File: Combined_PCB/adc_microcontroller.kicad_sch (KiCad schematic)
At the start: 26 parts, among them J3 Conn_01x18_Pin, J5 Conn_01x18_Pin, U1 ADS1299IPAG, U2 MCP1640BT-I/CHY

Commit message: Semi-finalized PCB Layout final
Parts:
- removed C15, C4: 1uF, Capacitor_SMD:C_0805_2012Metric, symbol Device:C
- removed C18, C8: .1uF, Capacitor_SMD:C_0805_2012Metric, symbol Device:C
- added R4: 1M, Resistor_SMD:R_0805_2012Metric, symbol Device:R
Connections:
- net AVDD is gone; now on net 5v: C14.1, C17.1, U1.19 (AVDD@1), U1.21 (AVDD@1), U1.22 (AVDD@1), U1.54 (AVDD1), U1.56 (AVDD@1), U1.59 (AVDD@2)
- net 3v3: now also C3.1, C7.1, U1.35 (~{PWDN}), U1.48 (DVDD), U1.50 (DVDD), R4.2
- net 5v: now also C20.1, R3.2; no longer C20.2, R3.1
- net AGND: now also C20.2, U1.17 (SRB1), U1.18 (SRB2), U1.25 (VREFN), U1.31 (RESV1); no longer C20.1
- net DRDY: now also J5.16 (Pin_16); no longer J5.15 (Pin_15)
- net START: now also J3.11 (Pin_11)
- net VREFP: now also U1.24 (VREFP)
- net at R2.1, U2.4 (VFB): now also R3.1; no longer R3.2
- net DAISY_IN: now reaches U1.41 (DAISY_IN)
- net GPIO1: now reaches U1.42 (GPIO1)
- net GPIO1: now also J3.16 (Pin_16)
- net GPIO2: now reaches U1.44 (GPIO2)
- net GPIO2: now also J3.15 (Pin_15)
- net GPIO3: now reaches U1.45 (GPIO3)
- net GPIO3: now also J3.14 (Pin_14)
- net GPIO4: now reaches U1.46 (GPIO4)
- net GPIO4: now also J3.13 (Pin_13)
- net CLK: no longer names the net of U1.37 (CLK)
- removed net DVDD: C3.1, C7.1, U1.35 (~{PWDN}), U1.48 (DVDD), U1.50 (DVDD), U1.52 (CLKSEL)
- new net CLK_SEL: R4.1, U1.52 (CLKSEL)
- no-connect marks 39 -> 25
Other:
- moved on the sheet: C1, C10, C12, C13, C14, C16, C17, C19, C2, C20, C3, C5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

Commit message: Schematic and footprints complete
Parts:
- removed U2: MCP1640BT-I/CHY, SOT-23-6_MC_MCH, symbol 2025-03-06_16-07-10:MCP1640BT-I_CHY
- added U7: MCP1640BT-I/CHY, MCP1640:SOT-23-6_MC_MCH, symbol MCP1640BT:MCP1640BT-I_CHY
- J6: renamed from J3; footprint (none) -> Connector_PinHeader_2.54mm:PinHeader_1x18_P2.54mm_Vertical
- J7: renamed from J5; footprint (none) -> Connector_PinHeader_2.54mm:PinHeader_1x18_P2.54mm_Vertical
- L1: footprint (none) -> Inductor_SMD:L_0805_2012Metric
- R3: renamed from R2; footprint (none) -> Resistor_SMD:R_0805_2012Metric
- R4: renamed from R3; footprint (none) -> Resistor_SMD:R_0805_2012Metric
- renumbered C1 to C11, C14 to C13, C13 to C14, C17 to C15, C2 to C17, C19 to C18, C20 to C19, C3 to C6, C5 to C8, C6 to C9, R4 to R2, U1 to U6
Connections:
- net 3v3: now also U7.3 (EN), U7.6 (VIN)
- net 5v: now also U7.5 (VOUT)
- net AGND: now also U7.2 (GND)
- net at L1.1: now also U7.1 (SW)
- net at R3.1, R4.1: now also U7.4 (VFB)
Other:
- moved on the sheet: U6

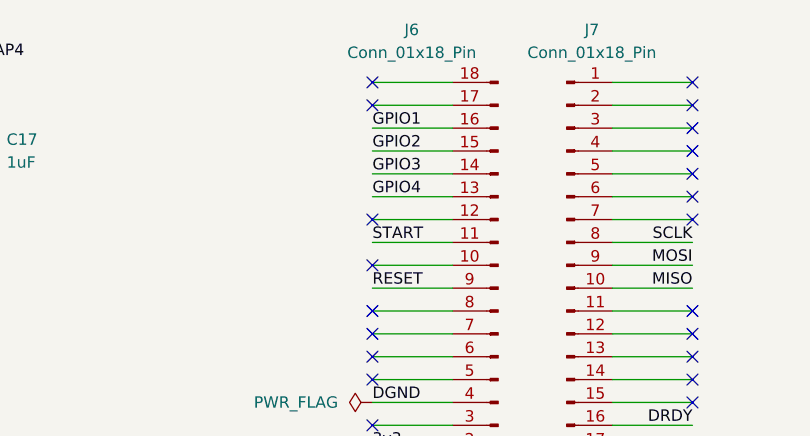
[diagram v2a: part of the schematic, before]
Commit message: ADS1299 final pcb layout done (hopefully)
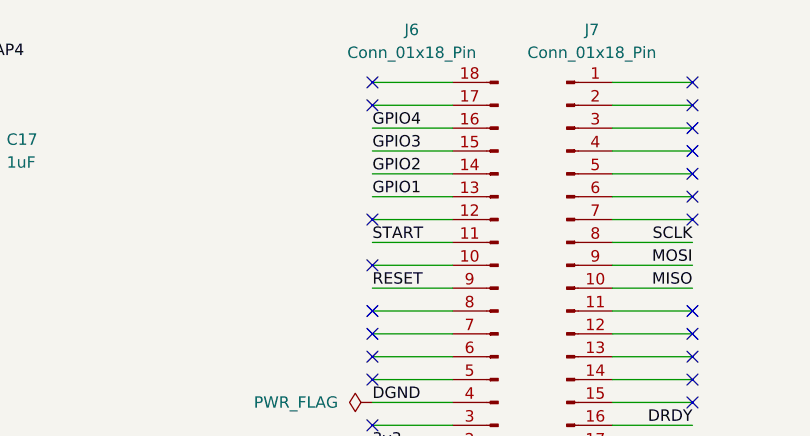
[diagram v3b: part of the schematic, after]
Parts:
- J6, J7: footprint Connector_PinHeader_2.54mm:PinHeader_1x18_P2.54mm_Vertical -> Connector_PinSocket_2.54mm:PinSocket_1x18_P2.54mm_Vertical
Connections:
- net GPIO1: now also J6.13 (Pin_13); no longer J6.16 (Pin_16)
- net GPIO2: now also J6.14 (Pin_14); no longer J6.15 (Pin_15)
- net GPIO3: now also J6.15 (Pin_15); no longer J6.14 (Pin_14)
- net GPIO4: now also J6.16 (Pin_16); no longer J6.13 (Pin_13)
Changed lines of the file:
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@@
 	)
 	(label "GPIO4"
-		(at 220.98 40.64 0)
+		(at 220.98 33.02 0)
 		(effects
 			(font
@@
 	)
 	(label "GPIO1"
-		(at 220.98 33.02 0)
+		(at 220.98 40.64 0)
 		(effects
 			(font
@@
 	)
 	(label "GPIO2"
-		(at 220.98 35.56 0)
+		(at 220.98 38.1 0)
 		(effects
 			(font
@@
 	)
 	(label "GPIO3"
-		(at 220.98 38.1 0)
+		(at 220.98 35.56 0)
 		(effects
 			(font
@@
 			)
 		)
-		(property "Footprint" "Connector_PinHeader_2.54mm:PinHeader_1x18_P2.54mm_Vertical"
+		(property "Footprint" "Connector_PinSocket_2.54mm:PinSocket_1x18_P2.54mm_Vertical"
 			(at 242.57 48.26 0)
 			(effects
@@
 			)
 		)
-		(property "Footprint" "Connector_PinHeader_2.54mm:PinHeader_1x18_P2.54mm_Vertical"
+		(property "Footprint" "Connector_PinSocket_2.54mm:PinSocket_1x18_P2.54mm_Vertical"
 			(at 234.95 50.8 0)
 			(effects

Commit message: Add CS
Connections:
- net AGND: no longer U6.39 (~{CS})
- net START: now also J6.12 (Pin_12); no longer J6.11 (Pin_11)
- new net CS: J6.11 (Pin_11), U6.39 (~{CS})
- no-connect marks 25 -> 24
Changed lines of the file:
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@@
+	)
+	(no_connect
+		(at 220.98 55.88)
+	)
+	(no_connect
+		(at 220.98 48.26)
+	)
+	(no_connect
+		(at 220.98 53.34)
+	)
+	(no_connect
+		(at 256.54 30.48)
+	)
+	(no_connect
+		(at 256.54 43.18)
+	)
+	(no_connect
+		(at 220.98 71.12)
+	)
+	(no_connect
+		(at 256.54 63.5)
+	)
+	(no_connect
+		(at 256.54 60.96)
+	)
+	(no_connect
+		(at 220.98 27.94)
+	)
+	(no_connect
+		(at 256.54 27.94)
+	)
+	(no_connect
+		(at 256.54 35.56)
+	)
+	(no_connect
+		(at 33.02 69.85)
 	)
 	(no_connect
 		(at 256.54 40.64)
-	)
-	(no_connect
-		(at 220.98 55.88)
-	)
-	(no_connect
-		(at 220.98 48.26)
-	)
-	(no_connect
-		(at 220.98 53.34)
-	)
-	(no_connect
-		(at 256.54 30.48)
-	)
-	(no_connect
-		(at 256.54 43.18)
-	)
-	(no_connect
-		(at 220.98 71.12)
-	)
-	(no_connect
-		(at 256.54 63.5)
-	)
-	(no_connect
-		(at 256.54 60.96)
-	)
-	(no_connect
-		(at 220.98 27.94)
-	)
-	(no_connect
-		(at 256.54 27.94)
-	)
-	(no_connect
-		(at 256.54 35.56)
-	)
-	(no_connect
-		(at 33.02 69.85)
-	)
-	(no_connect
-		(at 220.98 43.18)
 	)
 	(no_connect
@@
 		)
 	)
+	(label "CS"
+		(at 220.98 45.72 0)
+		(effects
+			(font
+				(size 1.27 1.27)
+			)
+			(justify left bottom)
+		)
+	)
 	(label "GPIO4"
 		(at 86.36 138.43 180)
@@
 	)
 	(label "START"
-		(at 220.98 45.72 0)
+		(at 220.98 43.18 0)
 		(effects
 			(font
@@
 		)
 	)
-	(label "AGND"
+	(label "CS"
 		(at 33.02 54.61 0)
 		(effects

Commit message: Final PCB Render Done
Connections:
- net AGND: no longer U6.17 (SRB1), U6.18 (SRB2)
- new net SRB1: U6.17 (SRB1)
- new net SRB2: U6.18 (SRB2)
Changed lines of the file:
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@@
 		)
 	)
-	(label "AGND"
+	(label "SRB1"
 		(at 33.02 143.51 0)
 		(effects
@@
 		)
 	)
-	(label "AGND"
+	(label "SRB2"
 		(at 33.02 146.05 0)
 		(effects
